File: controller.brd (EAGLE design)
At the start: 100 x 100 mm, 54 parts, among them IC1 7805DT, Q2 MOSFET-NCHANNELBSS123LT1G, Q3 MOSFET-NCHANNELFDD8780, U1 ATMEGA328P, Y1 16MHz

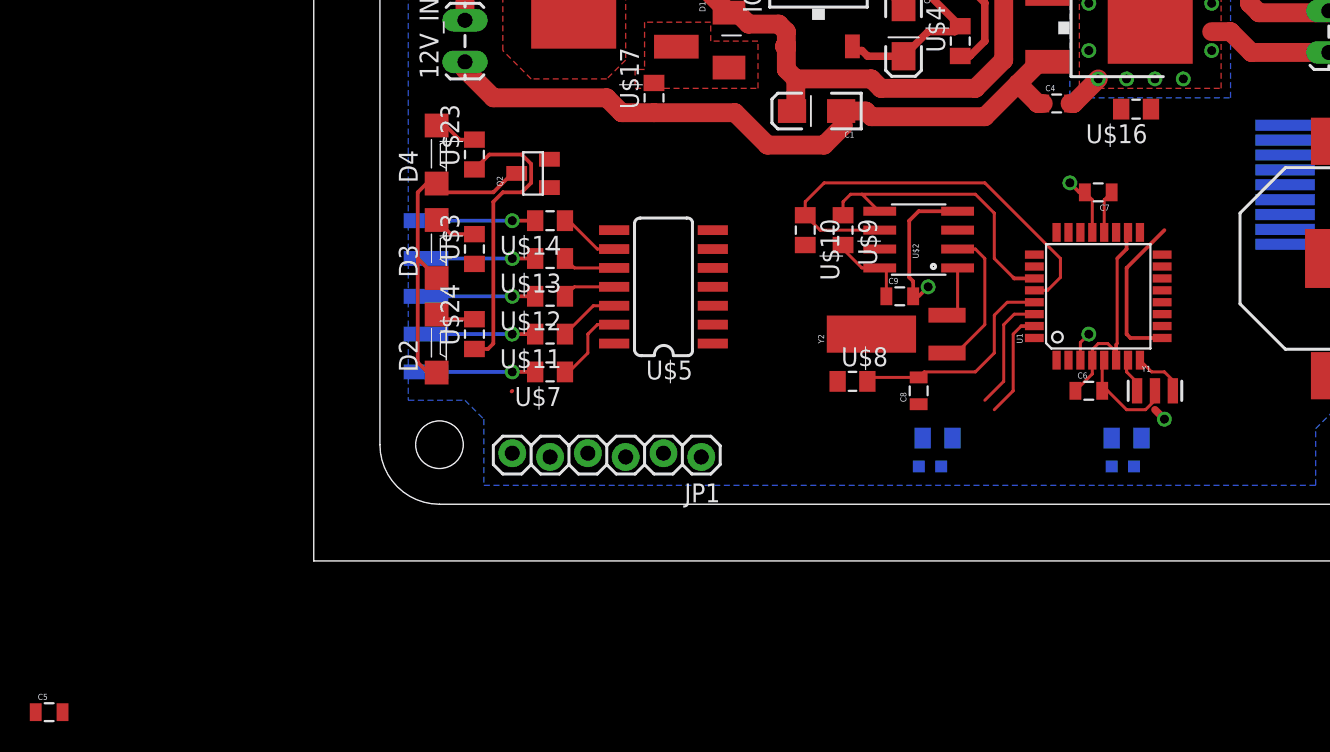
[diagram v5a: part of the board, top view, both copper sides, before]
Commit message: added sideview led footprint and replaced for night lights.
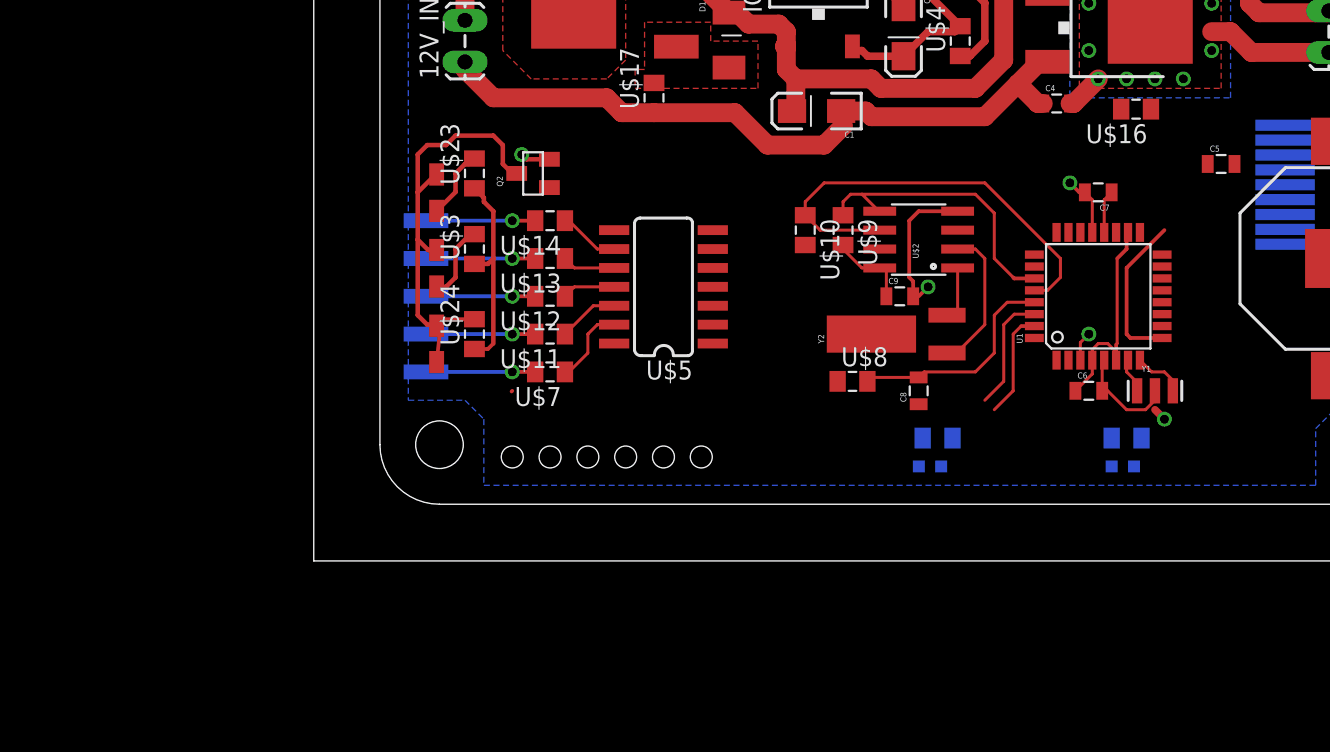
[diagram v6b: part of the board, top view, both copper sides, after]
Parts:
- D2, D3, D4: device adafruit:MICRO-SIDELED -> jt_parts:SIDEVIEW-LED
- JP1: device SparkFun-Connectors:1X06_LOCK -> SparkFun-Connectors:1X06_HOLES_ONLY
- moved C5 86.9 mm to (61.0, 26.7)
- moved D4 2.54 mm to (8.26, 24.8)
- moved D3 1.27 mm to (8.26, 19.7)
- moved U$23 1.27 mm to (10.8, 26.0)
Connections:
- net 12V: no longer U$18.1, U$21.1, U$22.1, U$23.1, U$24.1, U$3.1, U$6.1
- net 5V: now also U$18.1, U$21.1, U$22.1, U$23.1, U$24.1, U$3.1, U$6.1
- net N$12: now also D2.P$2, D3.P$2, D4.P$2; no longer D2.C, D3.C, D4.C
- net N$36: now also D2.P$1; no longer D2.A
- net N$37: now also D4.P$1; no longer D4.A
- net N$9: now also D3.P$1; no longer D3.A
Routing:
- net 12V: track 82.6 -> 62.9 mm
- net 5V: track 34.2 -> 48.0 mm
- net N$36: track 2.67 -> 5.13 mm
- net N$9: track 2.93 -> 5.13 mm
- net N$12: track 22.5 -> 24.7 mm
- net GND: track 91.7 -> 93.7 mm, vias 11 -> 12
- net N$37: track 3.38 -> 4.73 mm

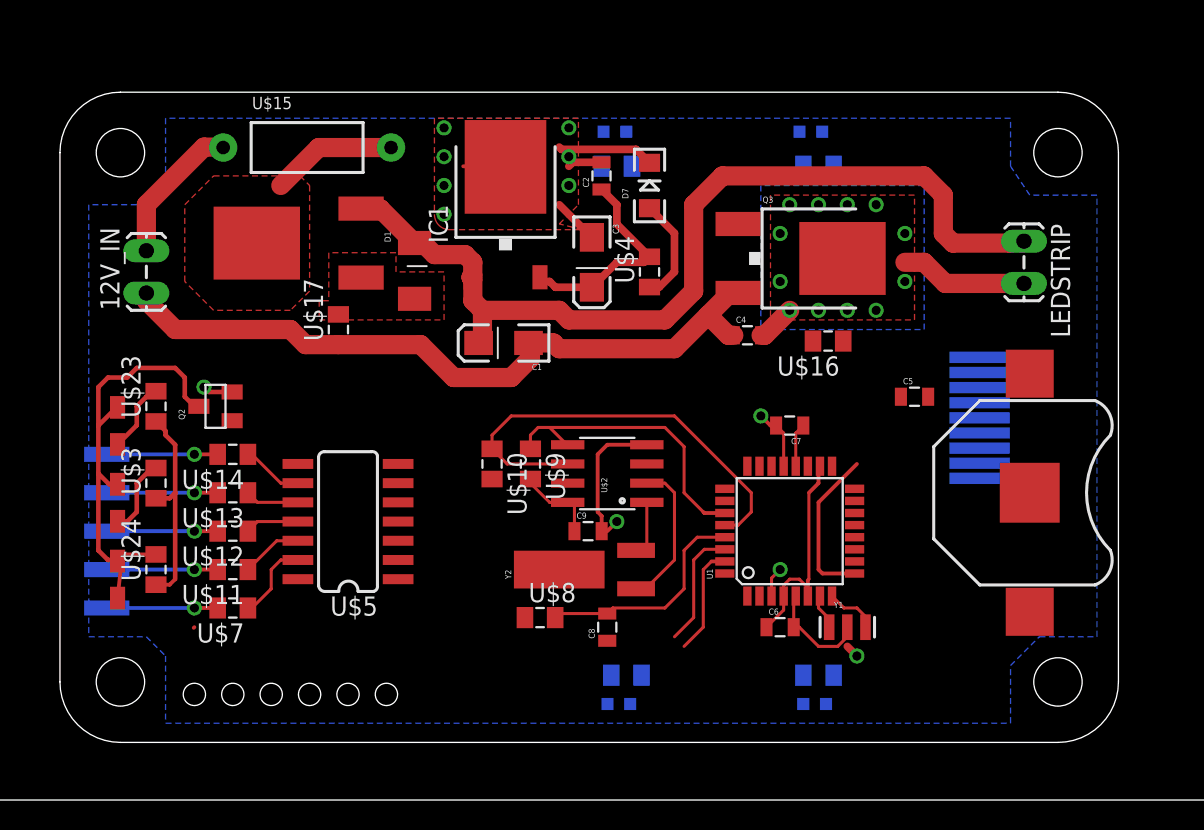
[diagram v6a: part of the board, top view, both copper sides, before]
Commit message: compacted layout. rerouted rtc. routed cap IC.
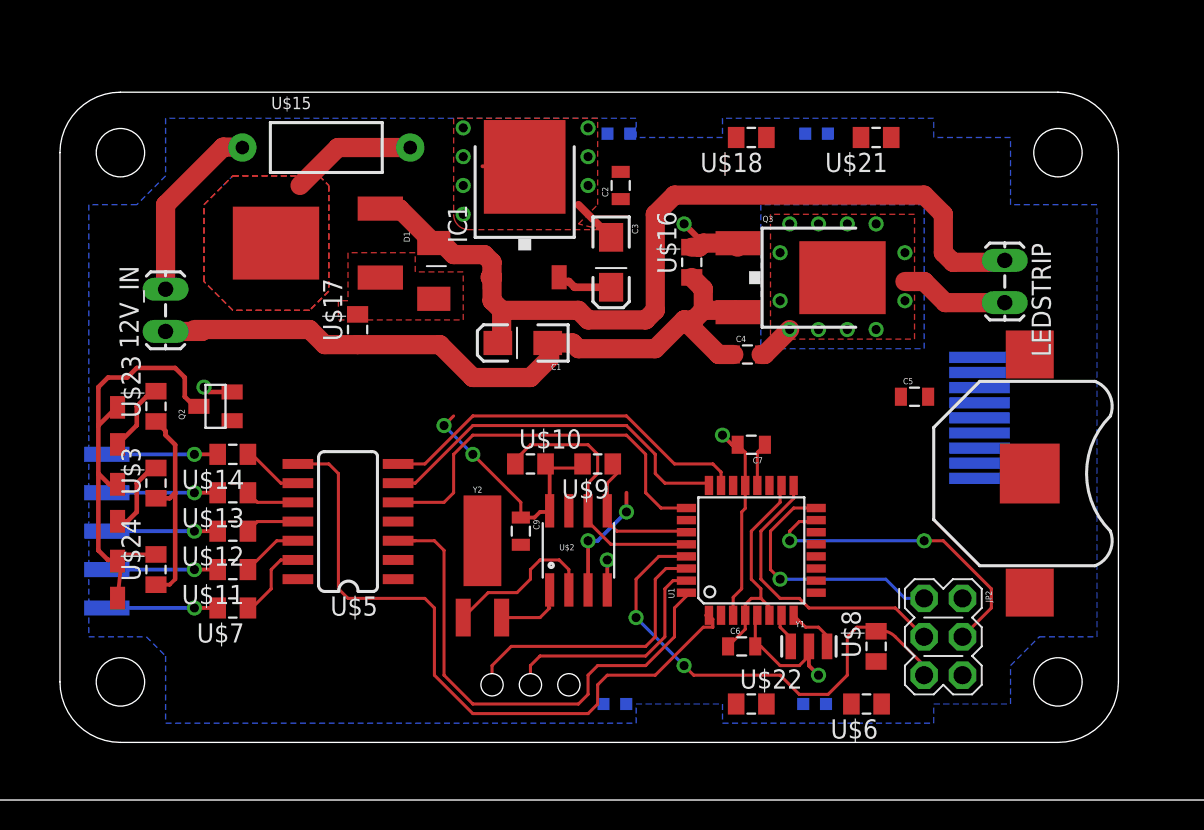
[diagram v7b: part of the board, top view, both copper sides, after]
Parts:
- removed C8: (no value), SparkFun-Capacitors:0805
- removed D7: GREEN, SparkFun-LED:LED-1206
- removed U$4: (no value), jt_parts:RESISTOR-0805
- added JP2: (no value), SparkFun-Connectors:2X3_POGO
- JP1: device SparkFun-Connectors:1X06_HOLES_ONLY -> SparkFun-Connectors:1X03_PP_HOLES_ONLY
- U$18, U$21, U$22, U$6: value 10k -> 103
- moved U$8 22.3 mm to (58.4, 10.2), turned to 90 degrees
- moved JP1 12.1 mm to (38.1, 7.62)
- moved Y2 10.6 mm to (32.4, 12.1), turned to 0 degrees
- moved U$16 10.4 mm to (46.2, 35.6), turned to 90 degrees
- moved U$18 9.09 mm to (50.2, 43.8), flipped to the top, turned to 180 degrees
- moved U$22 8.47 mm to (50.2, 6.35), flipped to the top
- moved U$2 5.43 mm to (38.7, 16.5), turned to 0 degrees
- moved C9 4.45 mm to (34.9, 17.8), turned to 270 degrees
- moved U$9 4.45 mm to (40.0, 22.2), turned to 180 degrees
- moved U$21 4.26 mm to (58.4, 43.8), flipped to the top, turned to 180 degrees
- moved U$6 3.70 mm to (57.8, 6.35), flipped to the top, turned to 180 degrees
- moved 12V_IN 2.84 mm to (11.4, 31.1)
- moved C6 2.84 mm to (49.5, 10.2)
- moved C7 2.84 mm to (50.2, 23.5)
- moved U1 2.84 mm to (50.2, 16.5)
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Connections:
- removed net DTR: C8.1, JP1.1
- removed net N$10: D7.A, U$4.1
- removed net N$15: C8.2, U$8.2, U1.29
- removed net VCC: NOKIA5110.1, NOKIA5110.6, U$10.2, U$9.2
- new net MISO: JP2.P$1, U1.16
- new net MOSI: JP2.P$4, U1.15
- new net RESET: JP2.P$5, U$8.2, U1.29
- new net SCK: JP2.P$3, U1.17
- net 5V: now also JP2.P$2, NOKIA5110.1, NOKIA5110.6, U$10.2, U$9.2; no longer JP1.4, U$4.2
- net GND: now also JP1.1, JP2.P$6; no longer D7.C, JP1.5, JP1.6
- net OUT0: now also U1.32
- net OUT1: now also U1.1; no longer U1.32
- net OUT2: now also U1.23; no longer U1.1
- net OUT3: now also U1.24
- net OUT4: now also U1.25
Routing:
- net OUT1: track 0.00 -> 45.6 mm
- net OUT0: track 0.00 -> 35.3 mm
- net RESET: track 0.00 -> 32.7 mm, vias 0 -> 2
- net OUT4: track 0.00 -> 25.9 mm
- net OUT2: track 0.00 -> 25.1 mm
- net OUT3: track 0.00 -> 24.5 mm
- net MOSI: track 0.00 -> 21.3 mm, vias 0 -> 2
- net SCK: track 0.00 -> 19.5 mm
- net MISO: track 0.00 -> 17.1 mm, vias 0 -> 1
- net N$15: track 14.9 -> 0.00 mm
- net SCL: track 29.5 -> 18.2 mm
- net RXI: track 7.96 -> 19.0 mm
- net SDA: track 19.8 -> 9.71 mm
- net TXO: track 7.25 -> 15.8 mm
- net VBATT: track 0.00 -> 7.85 mm, vias 0 -> 2
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- added copper zone on layer 16, net N$13

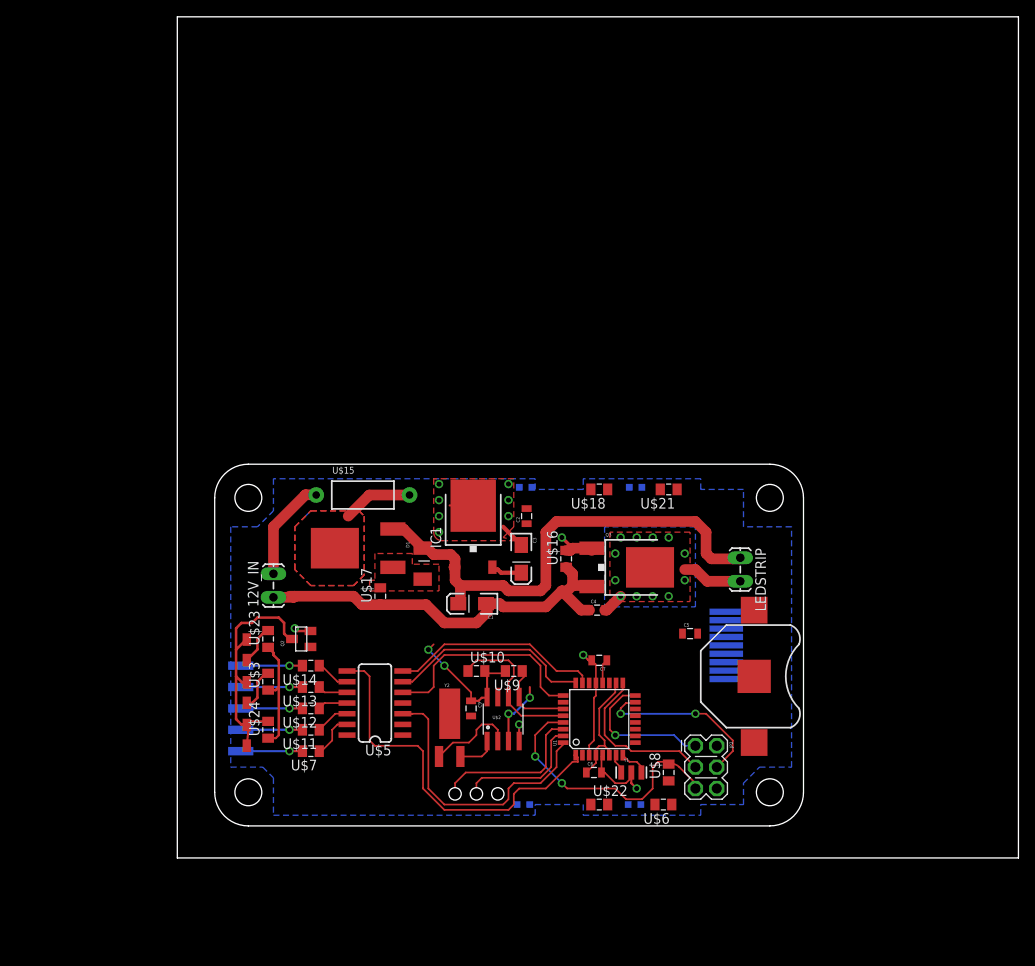
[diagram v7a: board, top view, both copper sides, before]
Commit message: put leds in series. continue to tweak layout.
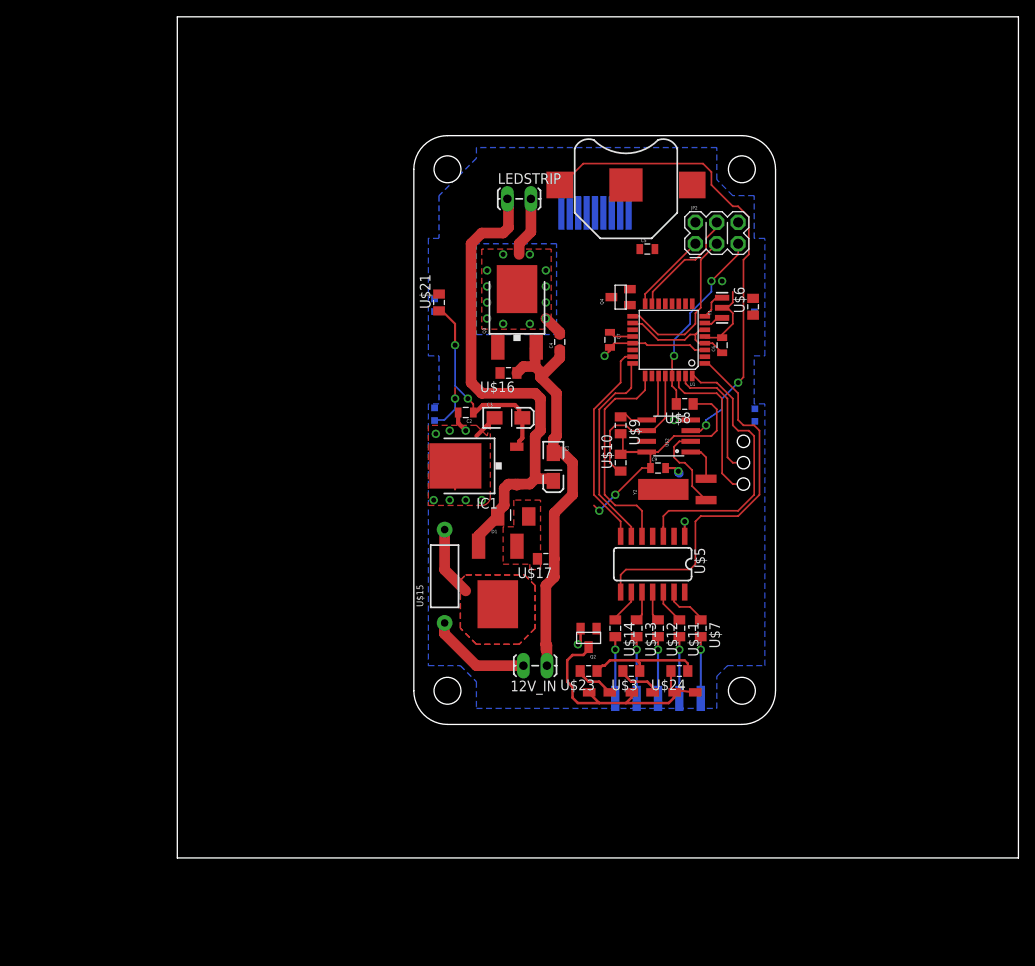
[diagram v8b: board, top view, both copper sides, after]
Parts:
- removed U$18, U$22: 103, jt_parts:RESISTOR-0805
- added Q4: MOSFET-NCHANNELBSS123LT1G, SparkFun-DiscreteSemi:SOT23
- moved U$20 67.8 mm to (71.1, 15.9), turned to 90 degrees
- moved LED4 61.0 mm to (68.6, 65.7), turned to 180 degrees
- moved BAT1 60.4 mm to (53.3, 80.0), turned to 0 degrees
- moved U$6 60.1 mm to (68.5, 65.5), turned to 90 degrees
- moved JP2 59.7 mm to (61.6, 73.0), turned to 0 degrees
- moved Y1 56.3 mm to (64.8, 65.4), turned to 90 degrees
- moved LED1 53.9 mm to (68.7, 52.7), turned to 180 degrees
- moved C6 53.0 mm to (64.8, 61.0), turned to 90 degrees
- moved D2 52.3 mm to (60.3, 19.7), turned to 90 degrees
- moved JP1 51.1 mm to (67.3, 49.5), turned to 270 degrees
- moved LEDSTRIP 50.9 mm to (39.4, 78.4), turned to 0 degrees
- moved U$19 49.5 mm to (57.1, 19.1), turned to 0 degrees
- moved U$24 49.4 mm to (59.7, 22.2), turned to 180 degrees
- moved U$7 48.6 mm to (62.2, 27.3), turned to 270 degrees
- moved D3 47.0 mm to (55.2, 19.7), turned to 90 degrees
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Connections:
- removed net LIGHT: Q2.1, U1.14
- removed net N$22: LED4.A, U$6.2
- removed net N$34: LED2.A, U$21.2
- removed net N$35: LED1.A, U$22.2
- new net BACK_LIGHT: Q4.1, U1.13
- new net N$10: Q4.3
- new net N$5: U$6.1
- new net NIGHT_LIGHT: Q2.1
- net 5V: no longer U$18.1, U$21.1, U$22.1, U$6.1
- net GND: now also Q4.2; no longer LED1.C, LED2.C, LED3.C, LED4.C
- net N$33: no longer U$18.2
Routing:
- net VBATT: track 7.85 -> 56.3 mm
- net 5V: track 48.6 -> 84.7 mm, vias 2 -> 4
- net RESET: track 32.7 -> 22.5 mm
- net MOSI: track 21.3 -> 13.6 mm, vias 2 -> 0
- net MISO: track 17.1 -> 9.61 mm, vias 1 -> 0
- net GND: track 85.9 -> 93.2 mm, vias 11 -> 13
- net PWM_LED: track 5.97 -> 0.37 mm, vias 1 -> 0
- net N$33: track 0.00 -> 5.55 mm, vias 0 -> 1
- net OUT1: track 45.6 -> 44.8 mm
